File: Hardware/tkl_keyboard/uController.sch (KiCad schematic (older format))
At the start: 14 parts, among them J3 Conn_02x03_Odd_Even, SW1 SW_Push, U5 ATmega32U4-AU, X2 KC2016K

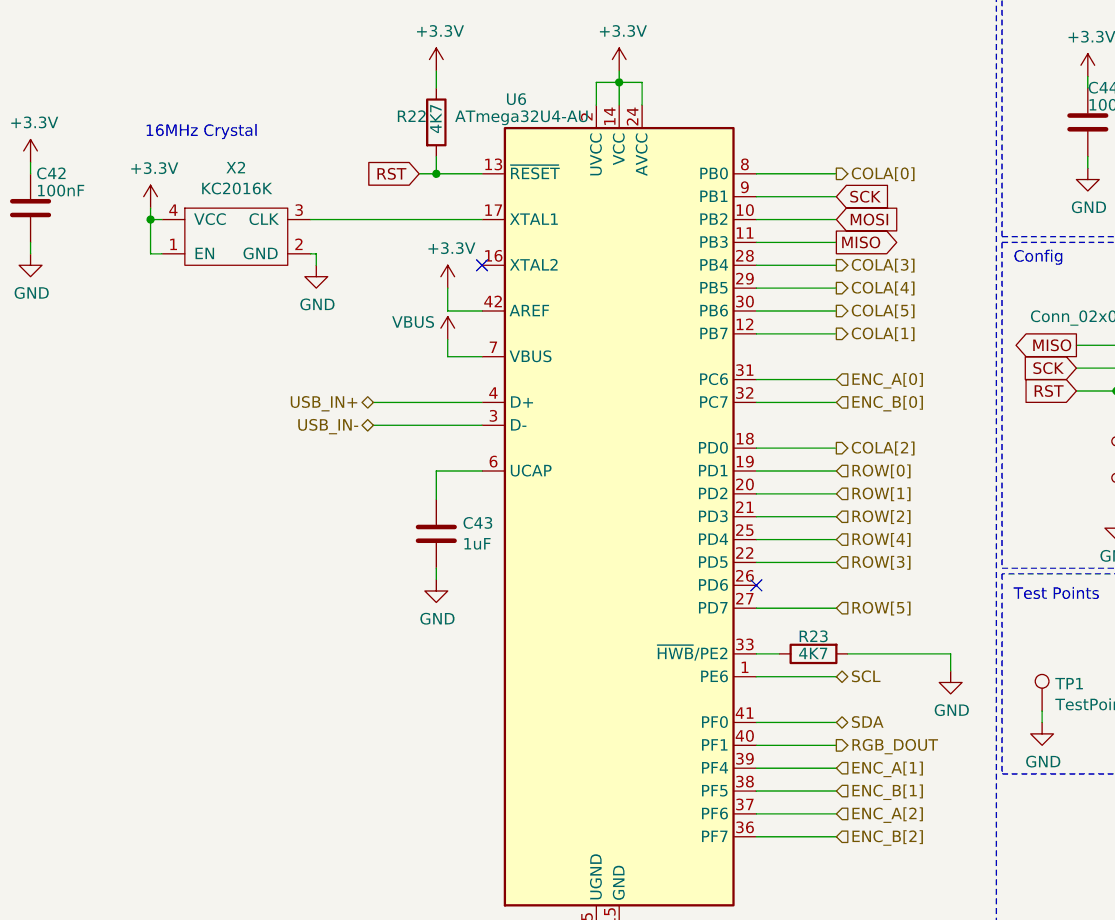
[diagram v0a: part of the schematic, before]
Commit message: Rows and columns routed to controller. Extended top board edge to fit OLED. Removed optional resistors around CMC.
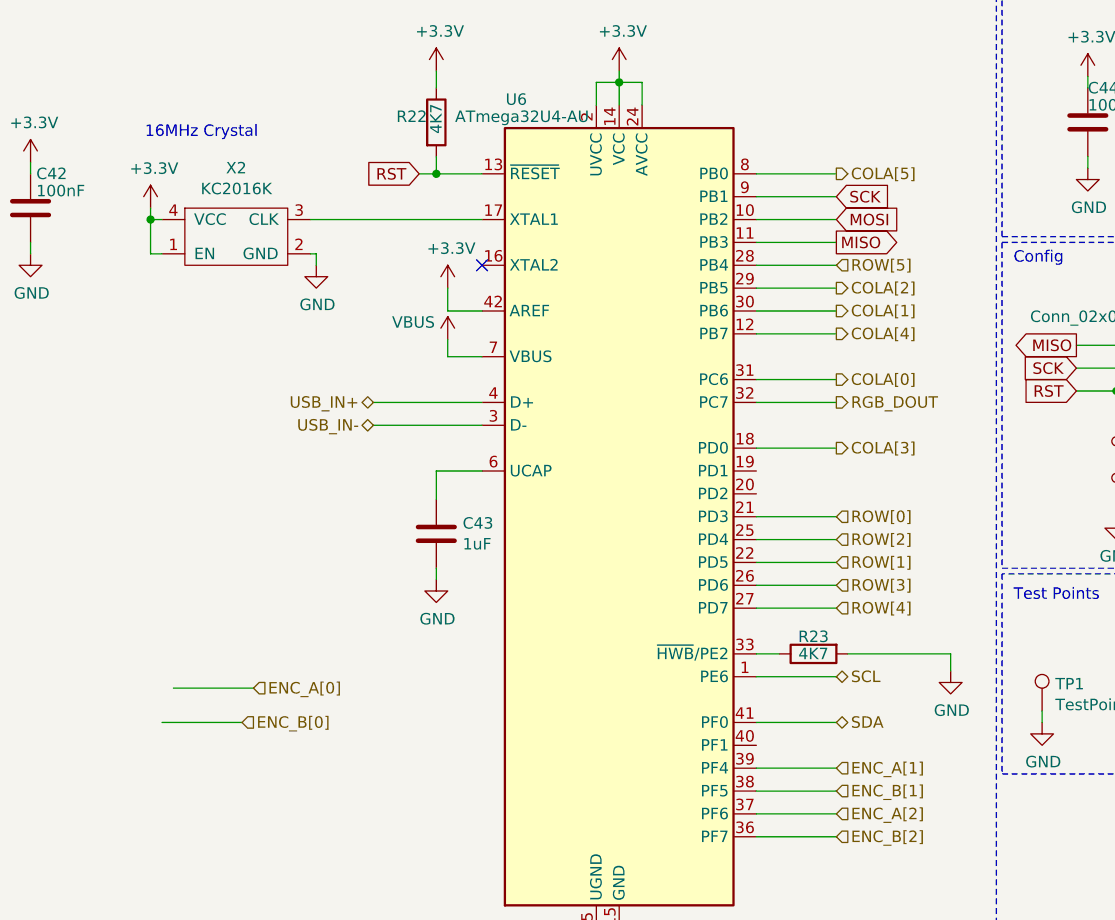
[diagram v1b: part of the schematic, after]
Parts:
- J3: footprint Connector_PinHeader_2.54mm:PinHeader_2x03_P2.54mm_Vertical_SMD -> custom_footprint_library:ISP_POGO
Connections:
- net COLA[0]: now also U5.31 (PC6); no longer U5.8 (PB0)
- net COLA[1]: now also U5.30 (PB6); no longer U5.12 (PB7)
- net COLA[2]: now also U5.29 (PB5); no longer U5.18 (PD0)
- net COLA[3]: now also U5.18 (PD0); no longer U5.28 (PB4)
- net COLA[4]: now also U5.12 (PB7); no longer U5.29 (PB5)
- net COLA[5]: now also U5.8 (PB0); no longer U5.30 (PB6)
- net ENC_A[0]: no longer U5.31 (PC6)
- net ENC_B[0]: no longer U5.32 (PC7)
- net RGB_DOUT: now also U5.32 (PC7); no longer U5.40 (PF1)
- net ROW[0]: now also U5.21 (PD3); no longer U5.19 (PD1)
- net ROW[1]: now also U5.22 (PD5); no longer U5.20 (PD2)
- net ROW[2]: now also U5.25 (PD4); no longer U5.21 (PD3)
- net ROW[3]: now also U5.26 (PD6); no longer U5.22 (PD5)
- net ROW[4]: now also U5.27 (PD7); no longer U5.25 (PD4)
- net ROW[5]: now also U5.28 (PB4); no longer U5.27 (PD7)
- no-connect marks 2 -> 1
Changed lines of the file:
@@
 	4975 5975 4975 6025
 Wire Wire Line
-	5575 4125 5925 4125
-Wire Wire Line
-	5575 3925 5925 3925
-Wire Wire Line
-	5575 3825 5925 3825
+	5575 4425 5925 4425
+Wire Wire Line
+	5575 4325 5925 4325
+Wire Wire Line
+	5575 3125 5925 3125
 $Comp
 L Device:C C?
@@
 	4175 2250 4175 2175
 Wire Wire Line
-	5575 3525 5925 3525
-Wire Wire Line
-	5575 3625 5925 3625
+	3025 4875 3375 4875
+Wire Wire Line
+	2975 5025 3325 5025
 Text Notes 750  1000 0    315  ~ 0
 uController
@@
 F 0 "J5" H 7400 3775 50  0000 C CNN
 F 1 "Conn_02x03_Odd_Even" H 7175 3700 50  0000 C CNN
-F 2 "Connector_PinHeader_2.54mm:PinHeader_2x03_P2.54mm_Vertical_SMD" H 7425 3475 50  0001 C CNN
+F 2 "custom_footprint_library:ISP_POGO" H 7425 3475 50  0001 C CNN
 F 3 "~" H 7425 3475 50  0001 C CNN
 	1    7425 3475
@@
 Config
 Wire Wire Line
-	5575 4025 5925 4025
+	5575 4225 5925 4225
 $Comp
 L power:VBUS #PWR?
@@
 	6650 2925 6650 4350
 Wire Wire Line
-	5925 4225 5575 4225
-Wire Wire Line
-	5925 5125 5575 5125
+	5925 3025 5575 3025
+Wire Wire Line
+	5925 3625 5575 3625
 Text Notes 2900 2475 0    50   ~ 0
 16MHz Crystal
@@
 	6425 4725 6425 4800
 Wire Wire Line
-	5925 4525 5575 4525
+	5925 4125 5575 4125
 Wire Wire Line
 	5925 5025 5575 5025
@@
 Connection ~ 2925 2825
 Wire Wire Line
-	5575 3325 5925 3325
-Wire Wire Line
-	5925 2625 5575 2625
-Wire Wire Line
-	5575 4325 5925 4325
-NoConn ~ 5575 4425
+	5575 3225 5925 3225
+Wire Wire Line
+	5925 3525 5575 3525
+Wire Wire Line
+	5575 4525 5925 4525
 Wire Notes Line
 	2250 6325 2250 1750
@@
 Text HLabel 5925 5025 2    50   BiDi ~ 0
 SDA
-Text HLabel 5925 5125 2    50   Output ~ 0
+Text HLabel 5925 3625 2    50   Output ~ 0
 RGB_DOUT
-Text HLabel 5925 3925 2    50   Input ~ 0
+Text HLabel 5925 4125 2    50   Input ~ 0
 ROW[0]
-Text HLabel 5925 4025 2    50   Input ~ 0
+Text HLabel 5925 4325 2    50   Input ~ 0
 ROW[1]
-Text HLabel 5925 4125 2    50   Input ~ 0
+Text HLabel 5925 4225 2    50   Input ~ 0
 ROW[2]
-Text HLabel 5925 4325 2    50   Input ~ 0
+Text HLabel 5925 4425 2    50   Input ~ 0
 ROW[3]
+Text HLabel 5925 3025 2    50   Input ~ 0
+ROW[5]
 Text HLabel 5925 4525 2    50   Input ~ 0
-ROW[5]
-Text HLabel 5925 4225 2    50   Input ~ 0
 ROW[4]
+Text HLabel 5925 3525 2    50   Output ~ 0
+COLA[0]
+Text HLabel 5925 3225 2    50   Output ~ 0
+COLA[1]
+Text HLabel 5925 3125 2    50   Output ~ 0
+COLA[2]
+Text HLabel 5925 3825 2    50   Output ~ 0
+COLA[3]
+Text HLabel 5925 3325 2    50   Output ~ 0
+COLA[4]
 Text HLabel 5925 2625 2    50   Output ~ 0
-COLA[0]
-Text HLabel 5925 3325 2    50   Output ~ 0
-COLA[1]
-Text HLabel 5925 3825 2    50   Output ~ 0
-COLA[2]
-Text HLabel 5925 3025 2    50   Output ~ 0
-COLA[3]
-Text HLabel 5925 3125 2    50   Output ~ 0
-COLA[4]
-Text HLabel 5925 3225 2    50   Output ~ 0
 COLA[5]
 Wire Wire Line
-	5925 3025 5575 3025
+	5925 3825 5575 3825
 Wire Wire Line
 	5925 2925 5575 2925
 Wire Wire Line
-	5925 3225 5575 3225
-Wire Wire Line
-	5925 3125 5575 3125
+	5925 2625 5575 2625
+Wire Wire Line
+	5925 3325 5575 3325
 Wire Wire Line
 	5575 5225 5925 5225
@@
 Wire Notes Line
 	6625 6325 6625 1750
-Text HLabel 5925 3525 2    50   Input ~ 0
+Text HLabel 3375 4875 2    50   Input ~ 0
 ENC_A[0]
-Text HLabel 5925 3625 2    50   Input ~ 0
+Text HLabel 3325 5025 2    50   Input ~ 0
 ENC_B[0]
 Text HLabel 5925 5225 2    50   Input ~ 0

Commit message: Updating schematic
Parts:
- R18, R19: value 4K7 -> 10K
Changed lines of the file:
@@
 $Descr A4 11693 8268
 encoding utf-8
-Sheet 4 11
+Sheet 4 12
 Title ""
 Date ""
@@
 AR Path="/63013830/60D6927E" Ref="R22"  Part="1"
 F 0 "R22" H 4000 2425 50  0000 L CNN
-F 1 "4K7" V 4175 2350 50  0000 L CNN
+F 1 "10K" V 4175 2350 50  0000 L CNN
 F 2 "resistor_smd:R_0603_1608Metric" V 4105 2400 50  0001 C CNN
 F 3 "~" H 4175 2400 50  0001 C CNN
@@
 AR Path="/63013830/6202A8FB" Ref="R23"  Part="1"
 F 0 "R23" V 5750 4725 50  0000 C CNN
-F 1 "4K7" V 5825 4725 50  0000 C CNN
+F 1 "10K" V 5825 4725 50  0000 C CNN
 F 2 "resistor_smd:R_0603_1608Metric" V 5755 4725 50  0001 C CNN
 F 3 "~" H 5825 4725 50  0001 C CNN

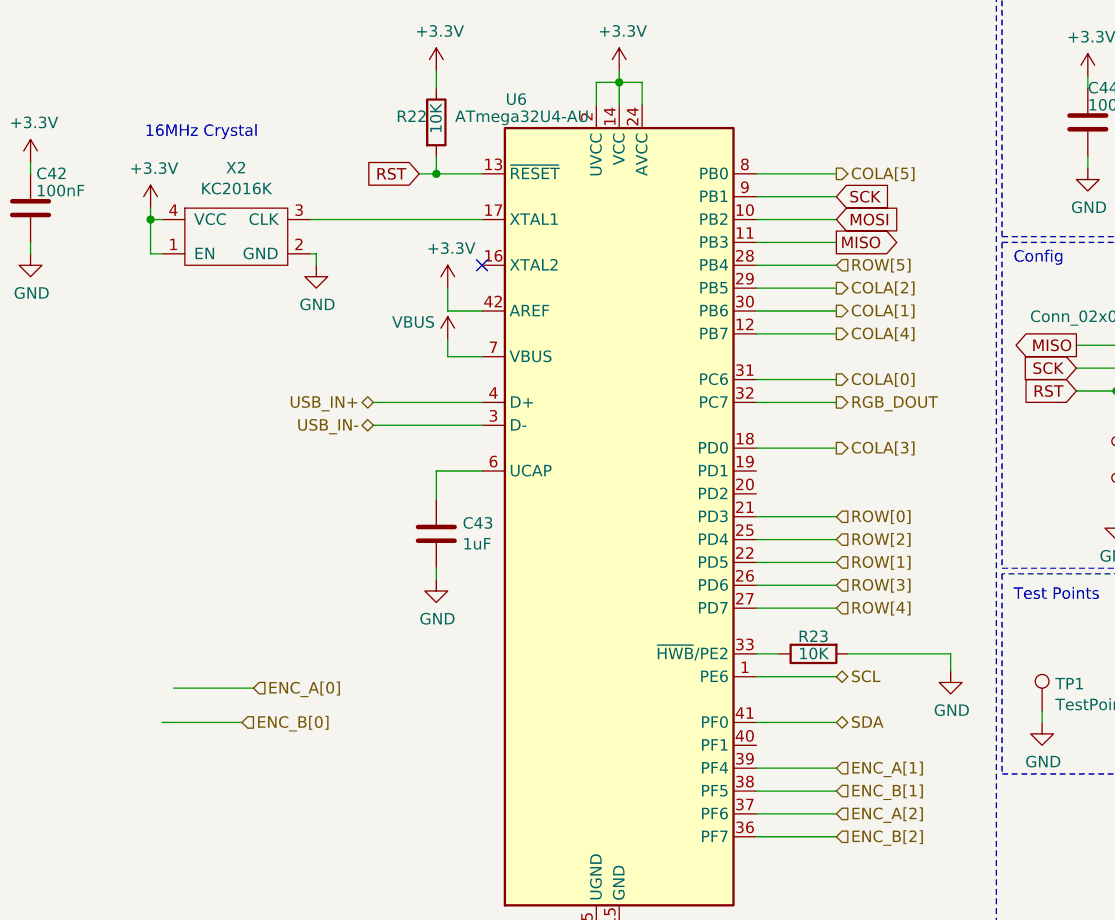
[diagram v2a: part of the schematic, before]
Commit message: Power supply routed
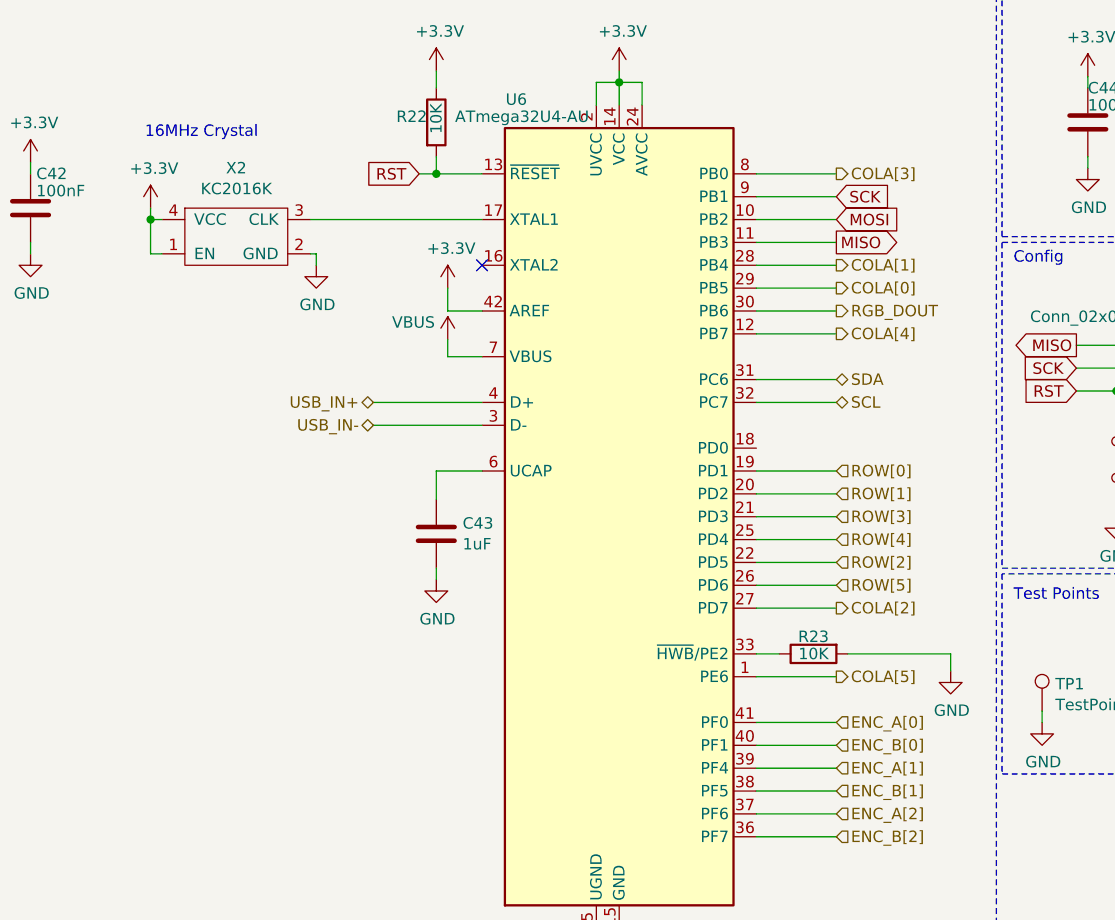
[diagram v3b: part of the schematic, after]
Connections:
- net COLA[0]: now also U5.29 (PB5); no longer U5.31 (PC6)
- net COLA[1]: now also U5.28 (PB4); no longer U5.30 (PB6)
- net COLA[2]: now also U5.27 (PD7); no longer U5.29 (PB5)
- net COLA[3]: now also U5.8 (PB0); no longer U5.18 (PD0)
- net COLA[5]: now also U5.1 (PE6); no longer U5.8 (PB0)
- net ENC_A[0]: now also U5.41 (PF0)
- net ENC_B[0]: now also U5.40 (PF1)
- net RGB_DOUT: now also U5.30 (PB6); no longer U5.32 (PC7)
- net ROW[0]: now also U5.19 (PD1); no longer U5.21 (PD3)
- net ROW[1]: now also U5.20 (PD2); no longer U5.22 (PD5)
- net ROW[2]: now also U5.22 (PD5); no longer U5.25 (PD4)
- net ROW[3]: now also U5.21 (PD3); no longer U5.26 (PD6)
- net ROW[4]: now also U5.25 (PD4); no longer U5.27 (PD7)
- net ROW[5]: now also U5.26 (PD6); no longer U5.28 (PB4)
- net SCL: now also U5.32 (PC7); no longer U5.1 (PE6)
- net SDA: now also U5.31 (PC6); no longer U5.41 (PF0)
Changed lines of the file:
@@
 	4975 5975 4975 6025
 Wire Wire Line
-	5575 4425 5925 4425
-Wire Wire Line
 	5575 4325 5925 4325
 Wire Wire Line
-	5575 3125 5925 3125
+	5575 4025 5925 4025
+Wire Wire Line
+	5575 4525 5925 4525
 $Comp
 L Device:C C?
@@
 	4175 2250 4175 2175
 Wire Wire Line
-	3025 4875 3375 4875
-Wire Wire Line
-	2975 5025 3325 5025
+	5575 5025 5925 5025
+Wire Wire Line
+	5575 5125 5925 5125
 Text Notes 750  1000 0    315  ~ 0
 uController
@@
 Config
 Wire Wire Line
-	5575 4225 5925 4225
+	5575 4125 5925 4125
 $Comp
 L power:VBUS #PWR?
@@
 	6650 2925 6650 4350
 Wire Wire Line
-	5925 3025 5575 3025
+	5925 4425 5575 4425
 Wire Wire Line
 	5925 3625 5575 3625
@@
 	6425 4725 6425 4800
 Wire Wire Line
-	5925 4125 5575 4125
-Wire Wire Line
-	5925 5025 5575 5025
-Wire Wire Line
-	5925 4825 5575 4825
+	5925 3925 5575 3925
+Wire Wire Line
+	5925 3225 5575 3225
+Wire Wire Line
+	5925 3525 5575 3525
 Wire Wire Line
 	3900 3625 4375 3625
@@
 Connection ~ 2925 2825
 Wire Wire Line
-	5575 3225 5925 3225
-Wire Wire Line
-	5925 3525 5575 3525
-Wire Wire Line
-	5575 4525 5925 4525
+	5575 3025 5925 3025
+Wire Wire Line
+	5925 3125 5575 3125
+Wire Wire Line
+	5575 4225 5925 4225
 Wire Notes Line
 	2250 6325 2250 1750
@@
 Text HLabel 3900 3725 0    50   BiDi ~ 0
 USB_IN-
-Text HLabel 5925 4825 2    50   BiDi ~ 0
+Text HLabel 5925 3625 2    50   BiDi ~ 0
 SCL
-Text HLabel 5925 5025 2    50   BiDi ~ 0
+Text HLabel 5925 3525 2    50   BiDi ~ 0
 SDA
-Text HLabel 5925 3625 2    50   Output ~ 0
+Text HLabel 5925 3225 2    50   Output ~ 0
 RGB_DOUT
+Text HLabel 5925 3925 2    50   Input ~ 0
+ROW[0]
+Text HLabel 5925 4025 2    50   Input ~ 0
+ROW[1]
+Text HLabel 5925 4325 2    50   Input ~ 0
+ROW[2]
 Text HLabel 5925 4125 2    50   Input ~ 0
-ROW[0]
-Text HLabel 5925 4325 2    50   Input ~ 0
-ROW[1]
+ROW[3]
+Text HLabel 5925 4425 2    50   Input ~ 0
+ROW[5]
 Text HLabel 5925 4225 2    50   Input ~ 0
-ROW[2]
-Text HLabel 5925 4425 2    50   Input ~ 0
-ROW[3]
-Text HLabel 5925 3025 2    50   Input ~ 0
-ROW[5]
-Text HLabel 5925 4525 2    50   Input ~ 0
 ROW[4]
-Text HLabel 5925 3525 2    50   Output ~ 0
+Text HLabel 5925 3125 2    50   Output ~ 0
 COLA[0]
-Text HLabel 5925 3225 2    50   Output ~ 0
+Text HLabel 5925 3025 2    50   Output ~ 0
 COLA[1]
-Text HLabel 5925 3125 2    50   Output ~ 0
+Text HLabel 5925 4525 2    50   Output ~ 0
 COLA[2]
-Text HLabel 5925 3825 2    50   Output ~ 0
+Text HLabel 5925 2625 2    50   Output ~ 0
 COLA[3]
 Text HLabel 5925 3325 2    50   Output ~ 0
 COLA[4]
-Text HLabel 5925 2625 2    50   Output ~ 0
+Text HLabel 5925 4825 2    50   Output ~ 0
 COLA[5]
 Wire Wire Line
-	5925 3825 5575 3825
+	5925 3325 5575 3325
 Wire Wire Line
 	5925 2925 5575 2925
 Wire Wire Line
+	5925 4825 5575 4825
+Wire Wire Line
 	5925 2625 5575 2625
 Wire Wire Line
-	5925 3325 5575 3325
-Wire Wire Line
 	5575 5225 5925 5225
 Wire Wire Line
@@
 Wire Notes Line
 	6625 6325 6625 1750
-Text HLabel 3375 4875 2    50   Input ~ 0
+Text HLabel 5925 5025 2    50   Input ~ 0
 ENC_A[0]
-Text HLabel 3325 5025 2    50   Input ~ 0
+Text HLabel 5925 5125 2    50   Input ~ 0
 ENC_B[0]
 Text HLabel 5925 5225 2    50   Input ~ 0
